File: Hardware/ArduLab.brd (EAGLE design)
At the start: 80 x 100 mm, 95 parts, among them CN1 USB-B, CN2 JST-PH, Q1 BSS138, Q2 BSS138, T1 MMUN2133LT1G, U1 ATMEGA32U4-AU, U2 MIC5205, U3 TPS61030PWP, U4 MCP73831, U5 L293DD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

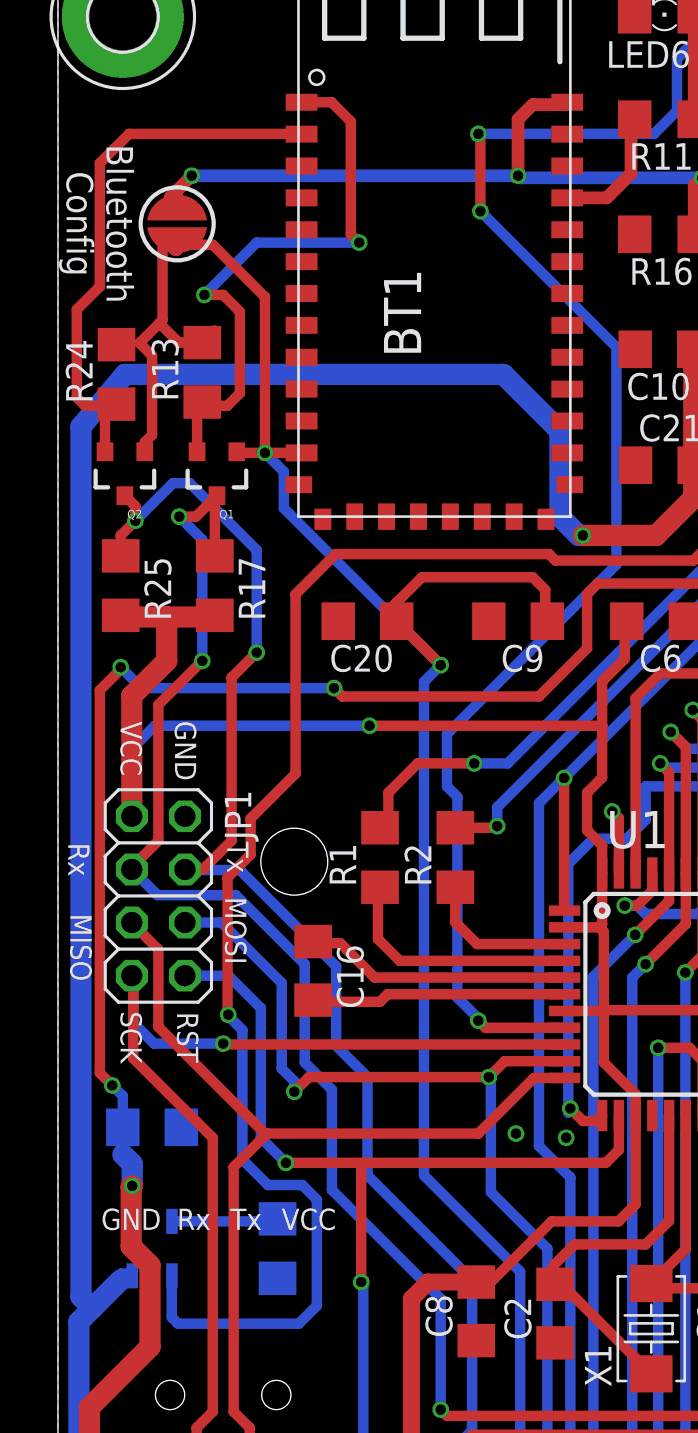
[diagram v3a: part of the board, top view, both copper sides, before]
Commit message: Added support for ESP8266-01
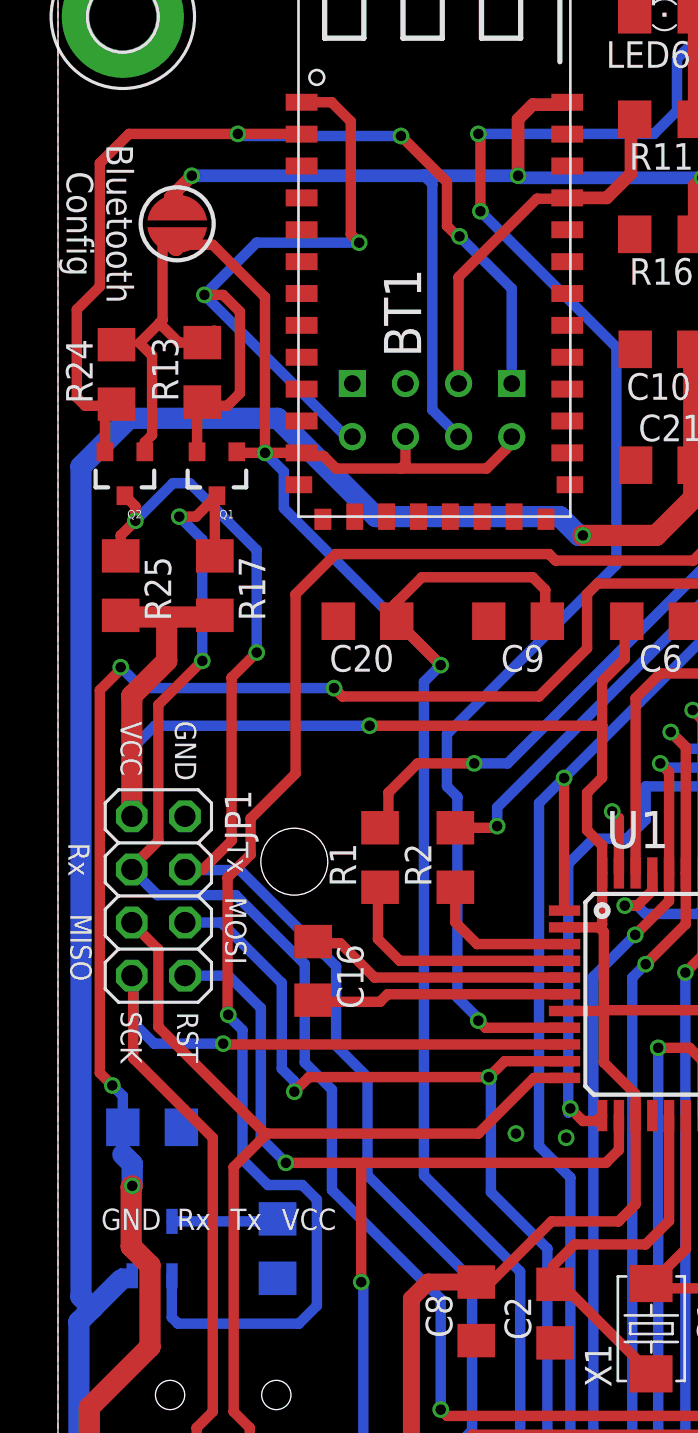
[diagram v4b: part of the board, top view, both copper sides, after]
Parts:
- added U$1: ESP01, esp8266modules:ESP01
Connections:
- removed net BRX: BT1.2, Q2.2, R24.1
- removed net BTX: BT1.1, Q1.2, R13.1
- removed net N$18: BT1.31, R11.2
- removed net N$24: BT1.34, R16.1, SJ2.1
- new net CL: BT1.31, R11.2, U$1.GPIO0
- new net CONF: BT1.34, R16.1, SJ2.1, U$1.RST
- new net RX: BT1.2, Q2.2, R24.1, U$1.RX
- new net TX: BT1.1, Q1.2, R13.1, U$1.TX
- net 3.3V: now also U$1.CH_PD, U$1.VCC
- net GND: now also U$1.GND
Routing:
- net RX: track 0.00 -> 48.9 mm, vias 0 -> 3
- net CONF: track 0.00 -> 47.6 mm, vias 0 -> 3
- net TX: track 0.00 -> 37.5 mm, vias 0 -> 2
- net N$24: track 34.5 -> 0.00 mm, vias 3 -> 0
- net BTX: track 27.7 -> 0.00 mm, vias 2 -> 0
- net BRX: track 26.5 -> 0.00 mm
- net CL: track 0.00 -> 18.1 mm
- net 3.3V: track 167.1 -> 179.9 mm
- net N$18: track 6.20 -> 0.00 mm
- net VBAT: track 178.2 -> 172.8 mm
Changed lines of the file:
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@@
 <element name="R24" library="resistor" package="R1206" value="10K" x="2.8" y="79.8" rot="R90"/>
 <element name="R25" library="resistor" package="R1206" value="10K" x="3" y="69.7" rot="R270"/>
+<element name="U$1" library="esp8266modules" package="ESP01" value="ESP01" x="17.9" y="85"/>
 </elements>
 <signals>
@@
 <contactref element="BT1" pad="14"/>
 <contactref element="BT1" pad="21"/>
+<contactref element="U$1" pad="GND"/>
 </signal>
 <signal name="AREF">
@@
 <wire x1="7.4" y1="86" x2="5.97" y2="86" width="0.5" layer="1"/>
 <wire x1="5.97" y1="86" x2="5.7" y2="85.73" width="0.5" layer="1"/>
+<contactref element="U$1" pad="VCC"/>
+<contactref element="U$1" pad="CH_PD"/>
+<wire x1="21.695" y1="76.8225" x2="21.695" y2="76.495" width="0.5" layer="1"/>
+<wire x1="21.695" y1="76.495" x2="20.5" y2="75.3" width="0.5" layer="1"/>
+<wire x1="20.5" y1="75.3" x2="16.4" y2="75.3" width="0.5" layer="1"/>
+<wire x1="16.4" y1="75.3" x2="13.3" y2="75.3" width="0.5" layer="1"/>
+<wire x1="13.3" y1="75.3" x2="12.7" y2="75.9" width="0.5" layer="1"/>
+<wire x1="12.7" y1="75.9" x2="11.798" y2="75.9" width="0.5" layer="1"/>
+<wire x1="11.798" y1="75.9" x2="11.65" y2="76.048" width="0.5" layer="1"/>
+<wire x1="16.615" y1="76.8225" x2="16.615" y2="75.515" width="0.5" layer="1"/>
+<wire x1="16.615" y1="75.515" x2="16.4" y2="75.3" width="0.5" layer="1"/>
 <wire x1="3.9" y1="81.3" x2="2.8" y2="81.222" width="0" layer="19" extent="1-1"/>
 </signal>
@@
 <wire x1="2.6" y1="45.8" x2="2" y2="46.4" width="0.5" layer="1"/>
 <wire x1="2" y1="46.4" x2="2" y2="64.7" width="0.5" layer="1"/>
-<wire x1="2" y1="64.7" x2="2" y2="65.6" width="0" layer="19" extent="1-16"/>
 <via x="13.2" y="64.8" extent="1-16" drill="0.5"/>
 <wire x1="13.2" y1="64.8" x2="13.6" y2="64.4" width="0.5" layer="1"/>
@@
 <wire x1="3.5" y1="36.9" x2="3" y2="36.9" width="0.3048" layer="16"/>
 <wire x1="3" y1="36.9" x2="3" y2="36.5" width="0.3048" layer="16"/>
-<wire x1="1.1" y1="77.3" x2="1.1" y2="35.7" width="1.016" layer="16"/>
+<wire x1="1.1" y1="75.4" x2="1.1" y2="35.7" width="1.016" layer="16"/>
 <wire x1="1.1" y1="35.7" x2="1.65" y2="35.15" width="1.016" layer="16"/>
 <wire x1="30.4" y1="81" x2="33.578" y2="81" width="1.016" layer="1"/>
@@
 <wire x1="25.1" y1="72.1" x2="24.9" y2="72.1" width="1.016" layer="16"/>
 <wire x1="24.9" y1="72.1" x2="24" y2="73" width="1.016" layer="16"/>
-<wire x1="24" y1="73" x2="24" y2="77.1" width="1.016" layer="16"/>
-<wire x1="24" y1="77.1" x2="21.3" y2="79.8" width="1.016" layer="16"/>
-<wire x1="21.3" y1="79.8" x2="3.2" y2="79.8" width="1.016" layer="16"/>
-<wire x1="3.2" y1="79.8" x2="1.1" y2="77.3" width="1.016" layer="16"/>
 <wire x1="51.576" y1="84.976" x2="48.4" y2="81.8" width="0.8128" layer="16"/>
 <wire x1="48.4" y1="81.8" x2="44.6" y2="81.8" width="0.8128" layer="16"/>
@@
 <wire x1="8" y1="23" x2="8" y2="20" width="1.016" layer="16"/>
 <wire x1="8" y1="20" x2="10.2" y2="20" width="1.016" layer="16"/>
+<wire x1="24" y1="73" x2="15.2" y2="73" width="1.016" layer="16"/>
+<wire x1="15.2" y1="73" x2="10.5" y2="77.7" width="1.016" layer="16"/>
+<wire x1="10.5" y1="77.7" x2="3.4" y2="77.7" width="1.016" layer="16"/>
+<wire x1="3.4" y1="77.7" x2="1.1" y2="75.4" width="1.016" layer="16"/>
 <wire x1="3.55" y1="36.85" x2="3.55" y2="36.6999" width="0" layer="19" extent="16-16"/>
 </signal>
@@
 <wire x1="66.7" y1="28.3" x2="65.5" y2="27.1" width="0.5" layer="1"/>
 </signal>
-<signal name="BTX">
+<signal name="TX">
 <contactref element="BT1" pad="1"/>
 <wire x1="11.65" y1="92.812" x2="13.088" y2="92.812" width="0.5" layer="1"/>
@@
 <wire x1="6.65" y1="76.1" x2="6.65" y2="78.228" width="0.5" layer="1"/>
 <wire x1="6.65" y1="78.228" x2="6.9" y2="78.478" width="0.5" layer="1"/>
-</signal>
-<signal name="BRX">
-<contactref element="BT1" pad="2"/>
-<wire x1="2" y1="84" x2="2" y2="89.9" width="0.5" layer="1"/>
-<wire x1="2" y1="89.9" x2="3.4" y2="91.3" width="0.5" layer="1"/>
-<wire x1="3.4" y1="91.3" x2="11.638" y2="91.3" width="0.5" layer="1"/>
-<wire x1="11.638" y1="91.3" x2="11.65" y2="91.288" width="0.5" layer="1"/>
-<contactref element="Q2" pad="2"/>
-<contactref element="R24" pad="1"/>
-<wire x1="2" y1="84" x2="0.9" y2="82.9" width="0.5" layer="1"/>
-<wire x1="0.9" y1="82.9" x2="0.9" y2="78.7" width="0.5" layer="1"/>
-<wire x1="0.9" y1="78.7" x2="1.3" y2="78.3" width="0.5" layer="1"/>
-<wire x1="1.3" y1="78.3" x2="2.722" y2="78.3" width="0.5" layer="1"/>
-<wire x1="2.722" y1="78.3" x2="2.8" y2="78.378" width="0.5" layer="1"/>
-<wire x1="2.25" y1="76.1" x2="2.25" y2="77.828" width="0.5" layer="1"/>
-<wire x1="2.25" y1="77.828" x2="2.8" y2="78.378" width="0.5" layer="1"/>
-</signal>
-<signal name="N$24">
+<contactref element="U$1" pad="TX"/>
+<wire x1="14.075" y1="76.8225" x2="13.7775" y2="76.8225" width="0.5" layer="16"/>
+<wire x1="13.7775" y1="76.8225" x2="7" y2="83.6" width="0.5" layer="16"/>
+</signal>
+<signal name="CONF">
 <contactref element="BT1" pad="34"/>
 <contactref element="R16" pad="1"/>
@@
 <wire x1="5.37" y1="88.27" x2="6.4" y2="89.3" width="0.6096" layer="1"/>
 <via x="6.4" y="89.3" extent="1-16" drill="0.5"/>
-<wire x1="6.4" y1="89.3" x2="22" y2="89.3" width="0.6096" layer="16"/>
-</signal>
-<signal name="N$18">
+<wire x1="6.4" y1="89.3" x2="17.5" y2="89.3" width="0.6096" layer="16"/>
+<contactref element="U$1" pad="RST"/>
+<wire x1="17.5" y1="89.3" x2="22" y2="89.3" width="0.6096" layer="16"/>
+<wire x1="19.155" y1="76.8225" x2="19.155" y2="76.845" width="0.5" layer="16"/>
+<wire x1="19.155" y1="76.845" x2="17.9" y2="78.1" width="0.5" layer="16"/>
+<wire x1="17.9" y1="78.1" x2="17.9" y2="88.9" width="0.5" layer="16"/>
+<wire x1="17.9" y1="88.9" x2="17.5" y2="89.3" width="0.5" layer="16"/>
+</signal>
+<signal name="CL">
 <contactref element="BT1" pad="31"/>
 <contactref element="R11" pad="2"/>
@@
 <wire x1="27.4" y1="89.4" x2="27.4" y2="91.822" width="0.6096" layer="1"/>
 <wire x1="27.4" y1="91.822" x2="27.578" y2="92" width="0.6096" layer="1"/>
+<contactref element="U$1" pad="GPIO0"/>
+<wire x1="19.155" y1="79.3625" x2="19.155" y2="84.455" width="0.5" layer="1"/>
+<wire x1="19.155" y1="84.455" x2="22.9" y2="88.2" width="0.5" layer="1"/>
+<wire x1="22.9" y1="88.2" x2="24.31" y2="88.2" width="0.5" layer="1"/>
+<wire x1="24.31" y1="88.2" x2="24.35" y2="88.24" width="0.5" layer="1"/>
 </signal>
 <signal name="N$19">
@@
 <wire x1="5.44" y1="36.6899" x2="5.45" y2="36.6999" width="0.5" layer="16"/>
 </signal>
+<signal name="RX">
+<contactref element="Q2" pad="2"/>
+<contactref element="R24" pad="1"/>
+<wire x1="2.25" y1="76.1" x2="2.25" y2="77.828" width="0.5" layer="1"/>
+<wire x1="2.25" y1="77.828" x2="2.8" y2="78.378" width="0.5" layer="1"/>
+<contactref element="U$1" pad="RX"/>
+<wire x1="21.695" y1="79.3625" x2="21.695" y2="83.905" width="0.5" layer="16"/>
+<wire x1="21.695" y1="83.905" x2="19.2" y2="86.4" width="0.5" layer="16"/>
+<via x="19.2" y="86.4" extent="1-16" drill="0.5"/>
+<wire x1="19.2" y1="86.4" x2="19.1" y2="86.4" width="0.5" layer="1"/>
+<wire x1="19.1" y1="86.4" x2="18.6" y2="86.9" width="0.5" layer="1"/>
+<wire x1="18.6" y1="86.9" x2="18.6" y2="89" width="0.5" layer="1"/>
+<wire x1="18.6" y1="89" x2="16.4" y2="91.2" width="0.5" layer="1"/>
+<via x="16.4" y="91.2" extent="1-16" drill="0.5"/>
+<wire x1="16.4" y1="91.2" x2="8.7" y2="91.2" width="0.5" layer="16"/>
+<wire x1="8.7" y1="91.2" x2="8.6" y2="91.3" width="0.5" layer="16"/>
+<via x="8.6" y="91.3" extent="1-16" drill="0.5"/>
+<wire x1="8.6" y1="91.3" x2="8.9" y2="91.3" width="0.5" layer="1"/>
+<wire x1="2.8" y1="78.378" x2="2.8" y2="78.4" width="0.5" layer="1"/>
+<wire x1="2.8" y1="78.4" x2="2.9" y2="78.4" width="0.5" layer="1"/>
+<wire x1="2.9" y1="78.4" x2="3" y2="78.5" width="0.5" layer="1"/>
+<contactref element="BT1" pad="2"/>
+<wire x1="2" y1="84" x2="2" y2="89.9" width="0.5" layer="1"/>
+<wire x1="2" y1="89.9" x2="3.4" y2="91.3" width="0.5" layer="1"/>
+<wire x1="3.4" y1="91.3" x2="11.638" y2="91.3" width="0.5" layer="1"/>
+<wire x1="11.638" y1="91.3" x2="11.65" y2="91.288" width="0.5" layer="1"/>
+<wire x1="2" y1="84" x2="0.9" y2="82.9" width="0.5" layer="1"/>
+<wire x1="0.9" y1="82.9" x2="0.9" y2="78.7" width="0.5" layer="1"/>
+<wire x1="0.9" y1="78.7" x2="1.3" y2="78.3" width="0.5" layer="1"/>
+<wire x1="1.3" y1="78.3" x2="2.722" y2="78.3" width="0.5" layer="1"/>
+<wire x1="11.638" y1="91.3" x2="8.9" y2="91.3" width="0" layer="19" extent="1-1"/>
+<wire x1="2.8" y1="78.4" x2="2.722" y2="78.3" width="0" layer="19" extent="1-1"/>
+</signal>
 </signals>

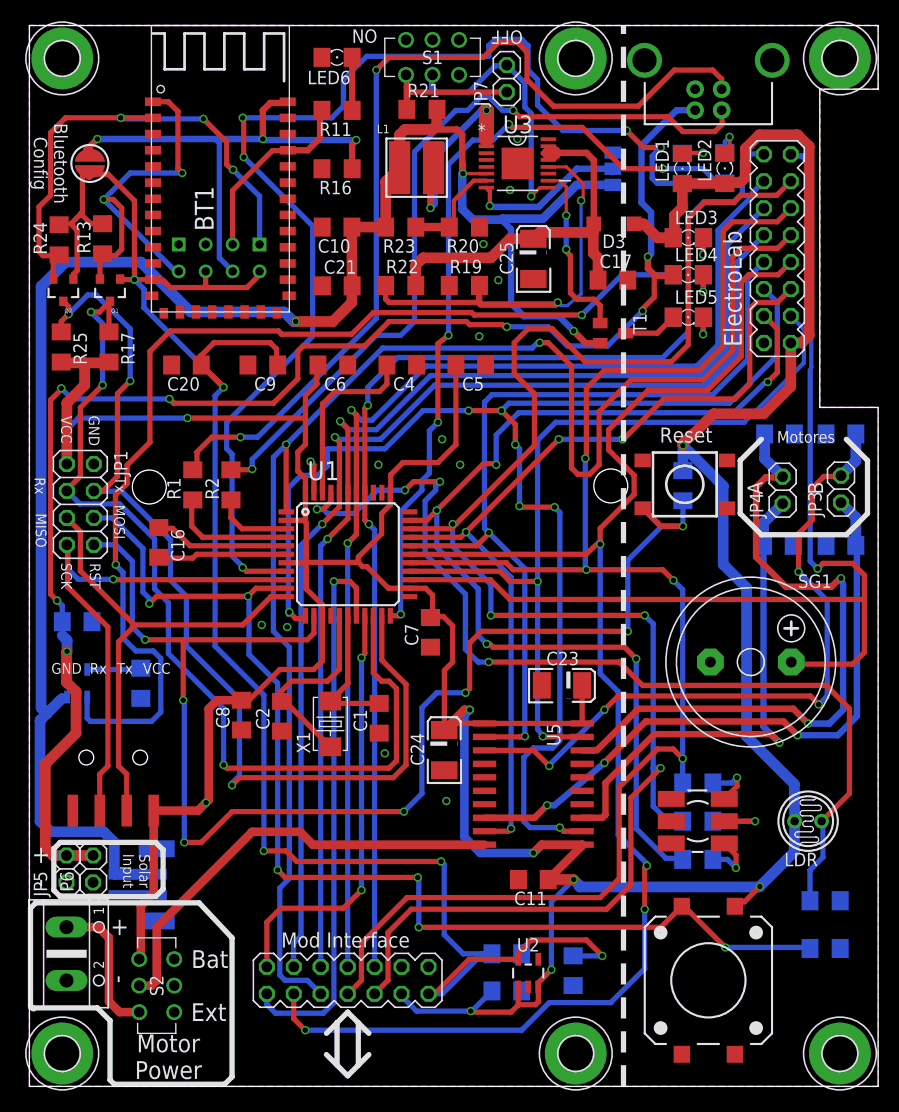
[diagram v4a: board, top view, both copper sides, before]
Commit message: LiPo power boosting circuit based in PAM2401 IC
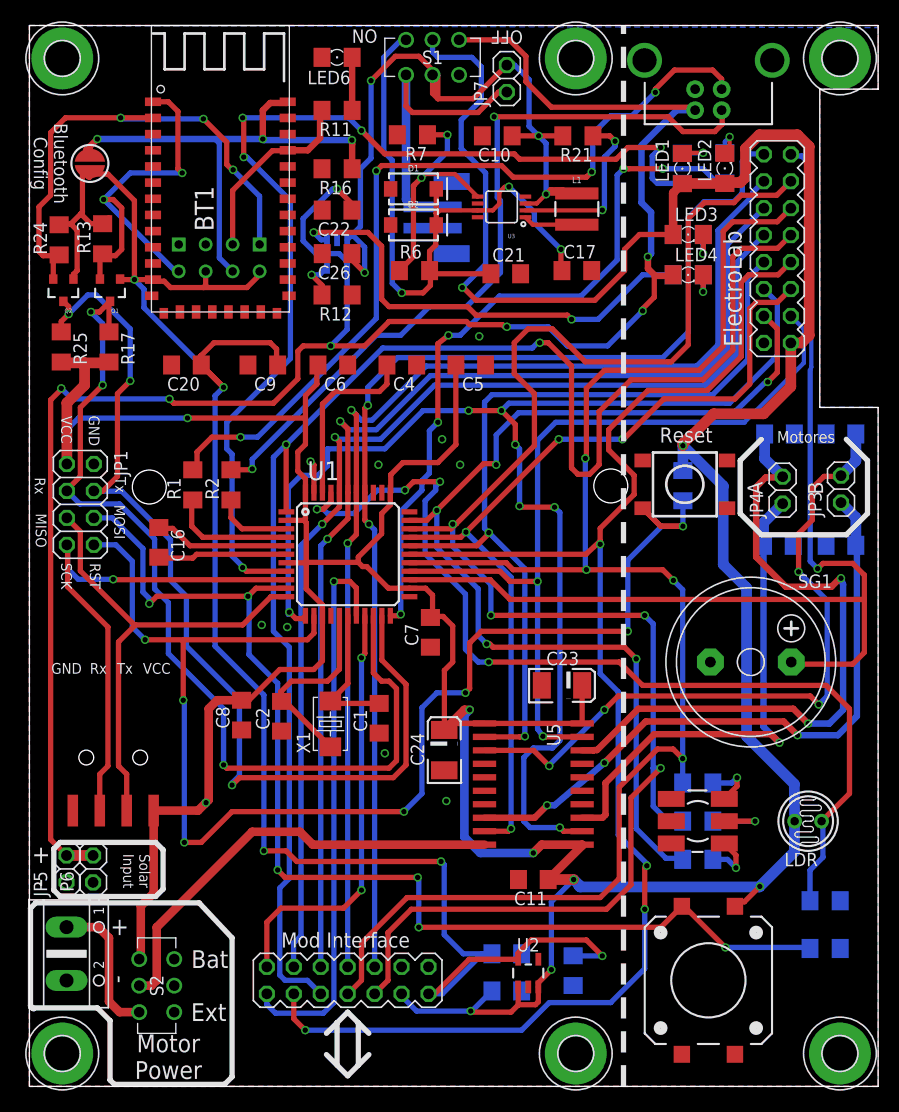
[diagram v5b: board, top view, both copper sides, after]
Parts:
- removed C25: 100uF, SparkFun:EIA3528-KIT
- removed D3: MBR120, diode:SOD123
- removed LED5: Red, led:1206
- removed R19: 200k, resistor:R1206
- removed R22, R23: 1.87M, resistor:R1206
- removed SJ1: PowerSave, jumper:SJ_2
- removed T1: MMUN2133LT1G, transistor:SC59-BEC
- added C26: 4.7uF, resistor:C1206
- added D1, D2: 3A/40V/500mV, SparkFun-DiscreteSemi:SMA-DIODE
- C10: value 100nF -> 22uF
- C17: value 2.2uF -> 22uF
- C21: value 10uF -> 22uF
- C22: value 10uF -> 4.7uF
- L1: value VLC5045-6.8uH -> 2.2UH3A; device microbuilder:INDUCTOR_5X5MM_TDK_VLC5045 -> SparkFun-Coils:INDUCTOR_4X4MM
- R20: value 340k -> 470
- R21: value 340k -> 750K
- R6: value 330 -> 750K
- R7: value 330 -> 100k
- U3: value TPS61030PWP -> PAM2401; device Texas Instruments_By_element14_Batch_1:SOP65P640X120-17N -> SparkFun-IC-Power:MSOP8
- moved CN2 68.8 mm to (39.8, 81.9)
- moved U4 47.3 mm to (29.0, 78.5), turned to 180 degrees
- moved C22 45.9 mm to (29.0, 82.6), flipped to the top
- moved R12 41.0 mm to (29.0, 74.6), flipped to the top, turned to 180 degrees
- moved R7 27.8 mm to (36.1, 89.7), flipped to the top
- moved R6 26.2 mm to (36.3, 76.9), flipped to the top, turned to 0 degrees
- moved R20 21.1 mm to (62.1, 80.3), flipped to the bottom
- moved C10 17.4 mm to (44.1, 89.6)
- moved C21 15.9 mm to (44.9, 76.6)
- moved L1 15.6 mm to (51.6, 82.7)
- moved R21 14.9 mm to (51.7, 89.6), turned to 180 degrees
- moved U3 4.37 mm to (44.5, 82.9), turned to 90 degrees
- moved C17 3.52 mm to (51.6, 76.9)
- moved LED3 0.30 mm to (62.1, 80.3)
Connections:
- removed net FB: R19.2, R22.1, U3.12
- removed net LBI: R20.2, R23.1, U3.7
- removed net LBO: T1.B, U3.10
- removed net N$17: LED3.C, R7.2
- removed net N$3: LED5.C, R6.2
- removed net SW: L1.P$2, U3.1, U3.2
- removed net SYNC: SJ1.2, U3.8
- new net N$14: LED3.C, R20.2
- new net VIN: C10.1, C26.1, JP7.2, L1.P$1, R21.2, S1.2, U3.3, U4.3
- net EN: now also R21.1, U3.2; no longer JP7.2, S1.2, U3.9
- net GND: now also C21.2, C26.2, D1.A, D2.A, R7.2, U3.8; no longer C21.1, C25.C, R19.1, R6.1, R7.1, SJ1.1, U3.11, U3.17, U3.3, U3.5
- net N$1: now also R6.1, R7.1, U3.5; no longer JP7.1, R21.1, S1.1
- net N$4: now also L1.P$2, U3.1; no longer LED5.A, T1.C
- net VBAT: now also JP7.1, S1.1; no longer C10.1, C21.2, L1.P$1, R21.2, R23.2, SJ1.3, T1.E, U3.6, U4.3
- net VBUS: now also S1.6
- net VCC: now also S1.5; no longer D3.C
- net VOUT: now also C21.1, D1.C, D2.C, R6.2, S1.4, U3.7; no longer C25.A, D3.A, R22.2, U3.13, U3.14, U3.15
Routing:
- net VBAT: track 172.8 -> 28.0 mm, vias 3 -> 0
- net VIN: track 0.00 -> 69.0 mm, vias 0 -> 4
- net N$11: track 100.3 -> 43.5 mm
- net VBUS: track 141.6 -> 184.0 mm
- net VCC: track 398.1 -> 437.3 mm, vias 9 -> 10
- net FB: track 36.8 -> 0.00 mm, vias 2 -> 0
- net VOUT: track 37.3 -> 62.5 mm, vias 0 -> 3
- net SW: track 19.0 -> 0.00 mm, vias 2 -> 0
- net LBO: track 17.1 -> 0.00 mm, vias 2 -> 0
- net SYNC: track 15.0 -> 0.00 mm, vias 1 -> 0
- net D17/PB0/RXLED: track 111.1 -> 99.6 mm
- net N$1: track 12.9 -> 22.9 mm, vias 0 -> 2
- net LBI: track 9.69 -> 0.00 mm
- net N$12: track 87.7 -> 78.8 mm, vias 2 -> 4
- net EN: track 24.8 -> 16.5 mm, vias 1 -> 2
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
